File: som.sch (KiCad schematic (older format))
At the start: 1 part, among them M1 SC606T

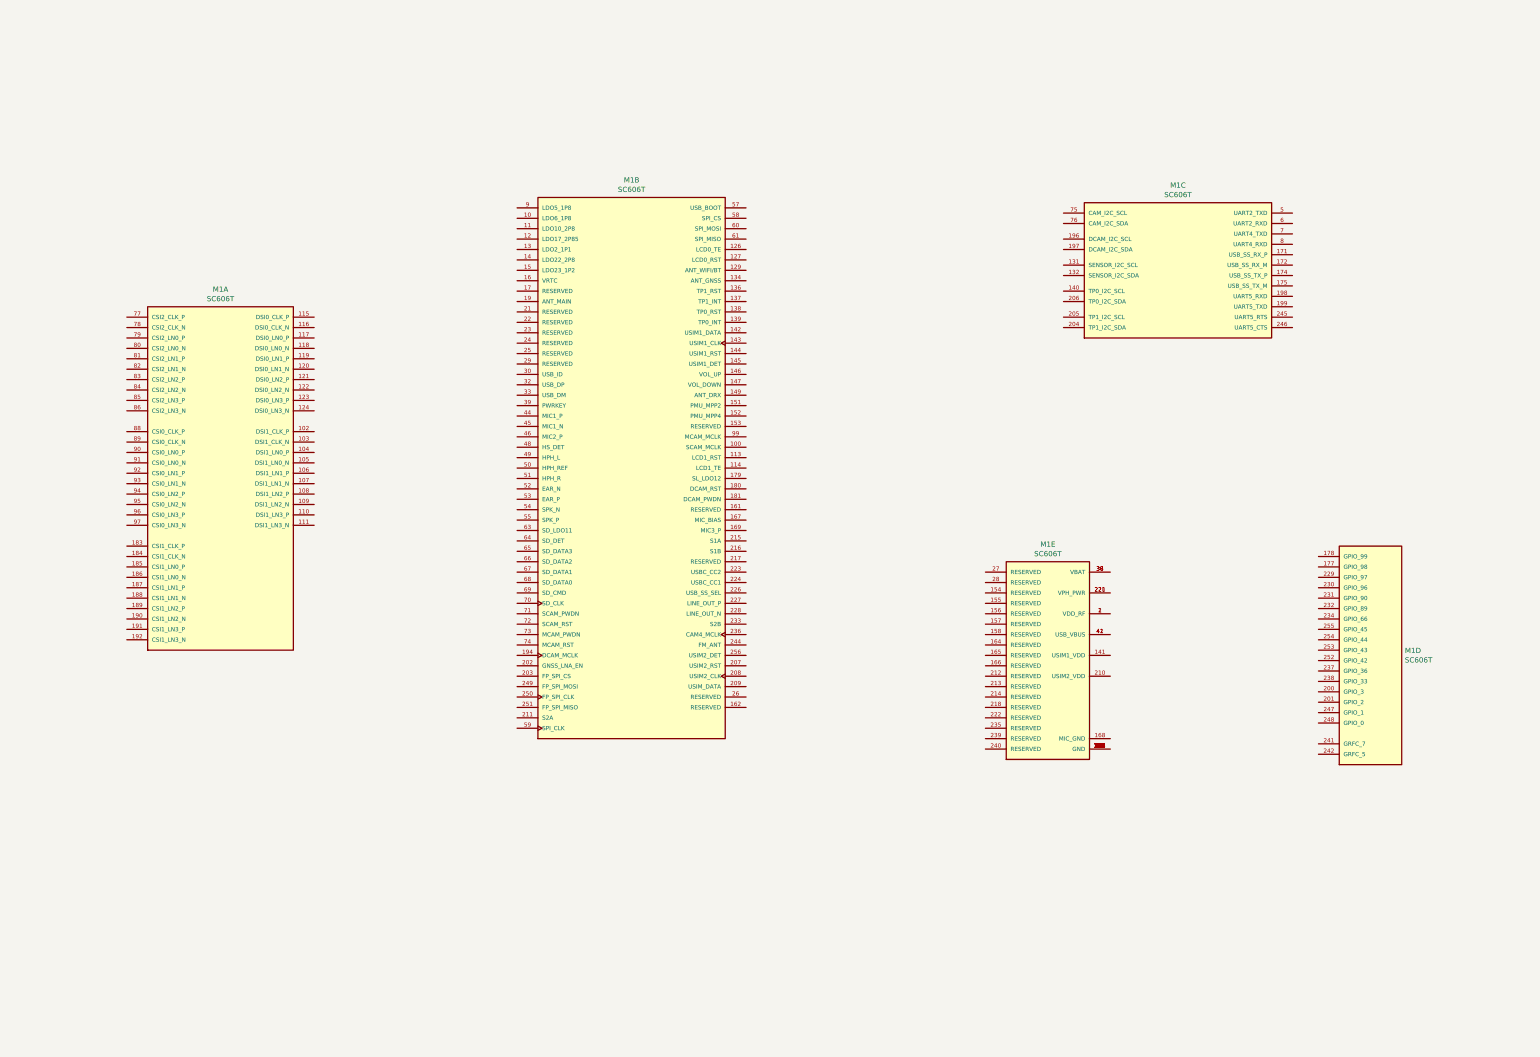
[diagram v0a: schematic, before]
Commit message: Creating schematic of SoM power supply elements
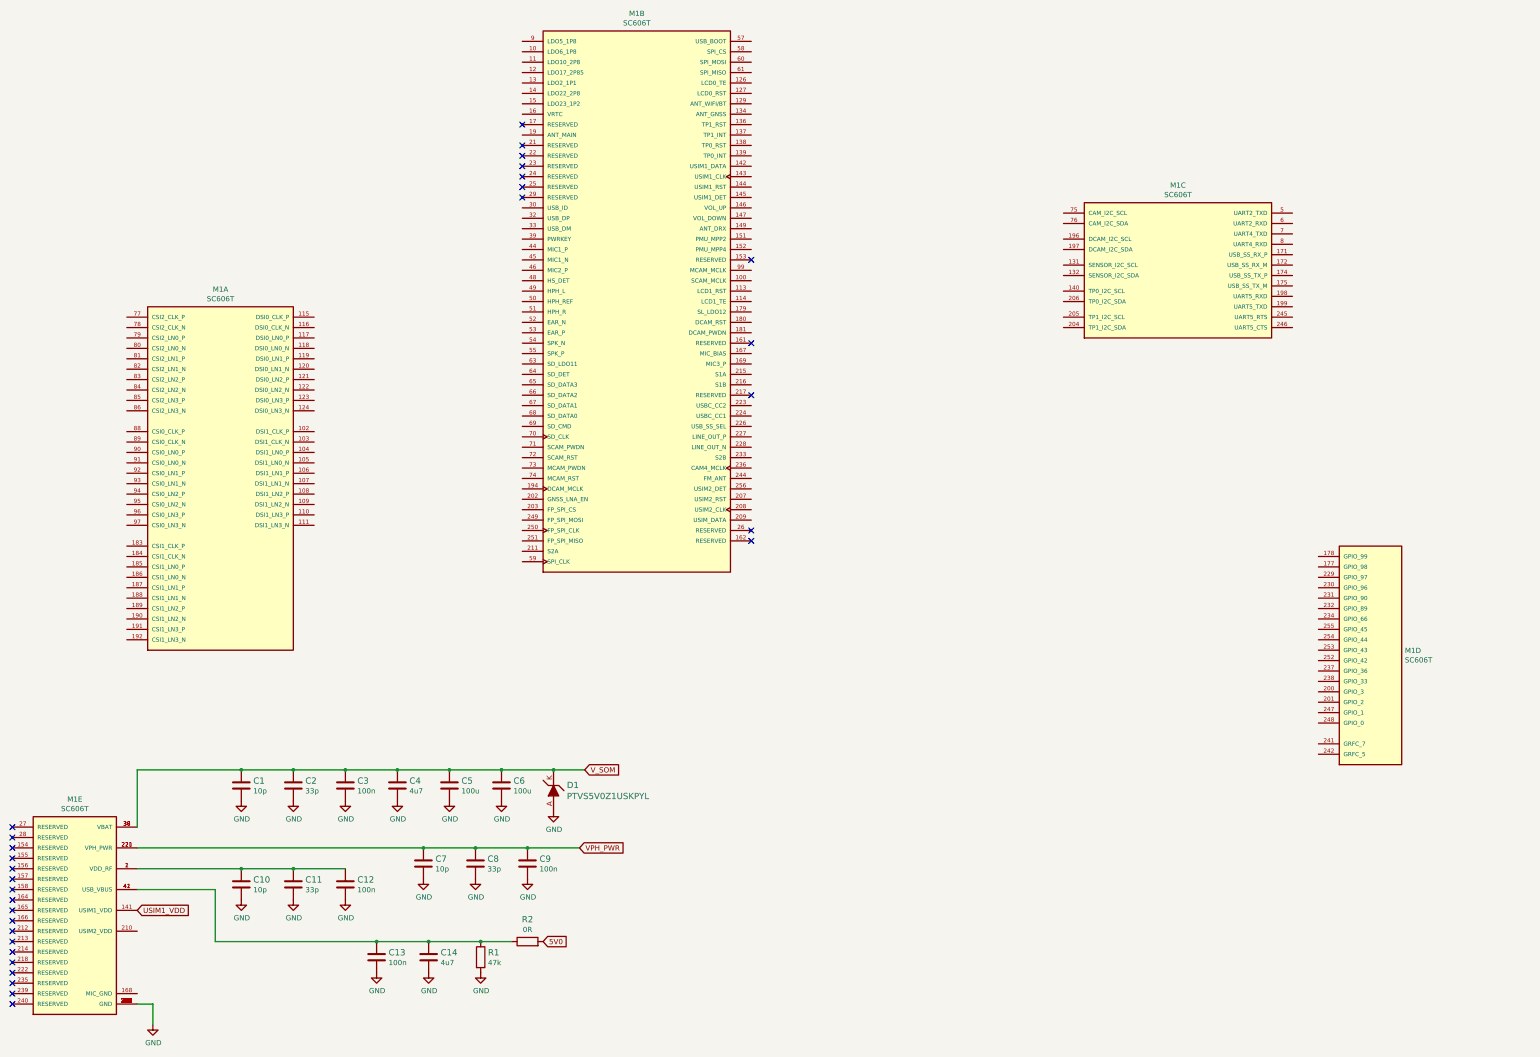
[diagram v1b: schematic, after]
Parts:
- added C1, C10, C7: C_10p_0402, antmicro-footprints:0402-cap, symbol antmicroCapacitors0402:C_10p_0402
- added C11, C2, C8: C_33p_0402, antmicro-footprints:0402-cap, symbol antmicroCapacitors0402:C_33p_0402
- added C12, C13, C3, C9: C_100n_0402, antmicro-footprints:0402-cap, symbol antmicroCapacitors0402:C_100n_0402
- added C14, C4: C_4u7_0402, antmicro-footprints:0402-cap, symbol antmicroCapacitors0402:C_4u7_0402
- added C5, C6: C_100u_1206, antmicro-footprints:1206-cap, symbol antmicroCapacitorsmisc:C_100u_1206
- added D1: PTVS5V0Z1USKPYL, antmicro-footprints:SOD-964, symbol antmicroTVSDiodes:PTVS5V0Z1USKPYL
- added R1: R_47k_0402, antmicro-footprints:0402-res, symbol antmicroResistors0402:R_47k_0402
- added R2: R_0R_0402, antmicro-footprints:0402-res, symbol antmicroResistors0402:R_0R_0402
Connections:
- net at M1.1 (VDD_RF), M1.2 (VDD_RF): now also C10.1, C11.1, C12.1
- net GND: now reaches M1.101 (GND), M1.112 (GND), M1.125 (GND), M1.128 (GND), M1.130 (GND), M1.133 (GND), M1.135 (GND), M1.148 (GND), M1.150 (GND), M1.159 (GND), M1.160 (GND), M1.163 (GND), M1.170 (GND), M1.173 (GND), M1.176 (GND), M1.18 (GND), M1.182 (GND), M1.193 (GND), M1.195 (GND), M1.20 (GND), M1.219 (GND), M1.225 (GND), M1.243 (GND), M1.257 (GND), M1.258 (GND), M1.259 (GND), M1.260 (GND), M1.261 (GND), M1.262 (GND), M1.263 (GND), M1.264 (GND), M1.265 (GND), M1.266 (GND), M1.267 (GND), M1.268 (GND), M1.269 (GND), M1.270 (GND), M1.271 (GND), M1.272 (GND), M1.273 (GND), M1.274 (GND), M1.275 (GND), M1.276 (GND), M1.277 (GND), M1.278 (GND), M1.279 (GND), M1.280 (GND), M1.281 (GND), M1.282 (GND), M1.283 (GND), M1.284 (GND), M1.285 (GND), M1.286 (GND), M1.287 (GND), M1.288 (GND), M1.289 (GND), M1.290 (GND), M1.291 (GND), M1.292 (GND), M1.293 (GND), M1.294 (GND), M1.295 (GND), M1.296 (GND), M1.297 (GND), M1.298 (GND), M1.299 (GND), M1.3 (GND), M1.300 (GND), M1.301 (GND), M1.302 (GND), M1.303 (GND), M1.304 (GND), M1.305 (GND), M1.306 (GND), M1.307 (GND), M1.308 (GND), M1.309 (GND), M1.31 (GND), M1.310 (GND), M1.311 (GND), M1.312 (GND), M1.313 (GND), M1.314 (GND), M1.315 (GND), M1.316 (GND), M1.317 (GND), M1.318 (GND), M1.319 (GND), M1.320 (GND), M1.321 (GND), M1.322 (GND), M1.323 (GND), M1.34 (GND), M1.35 (GND), M1.4 (GND), M1.40 (GND), M1.43 (GND), M1.47 (GND), M1.56 (GND), M1.62 (GND), M1.87 (GND), M1.98 (GND)
- net GND: now also C1.2, C10.2, C11.2, C12.2, C13.2, C14.2, C2.2, C3.2, C4.2, C5.2, C6.2, C7.2, C8.2, C9.2, D1.A, R1.2
- net USIM1_VDD: now reaches M1.141 (USIM1_VDD)
- net VPH_PWR: now reaches M1.220 (VPH_PWR), M1.221 (VPH_PWR)
- net VPH_PWR: now also C7.1, C8.1, C9.1
- net V_SOM: now reaches M1.36 (VBAT), M1.37 (VBAT), M1.38 (VBAT)
- net V_SOM: now also C1.1, C2.1, C3.1, C4.1, C5.1, C6.1, D1.K
- net at M1.41 (USB_VBUS), M1.42 (USB_VBUS): now also C13.1, C14.1, R1.1, R2.1
- new net 5V0: R2.2
- no-connect marks 0 -> 30
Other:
- moved on the sheet: M1B, M1E

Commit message: Add scheme for SIM card
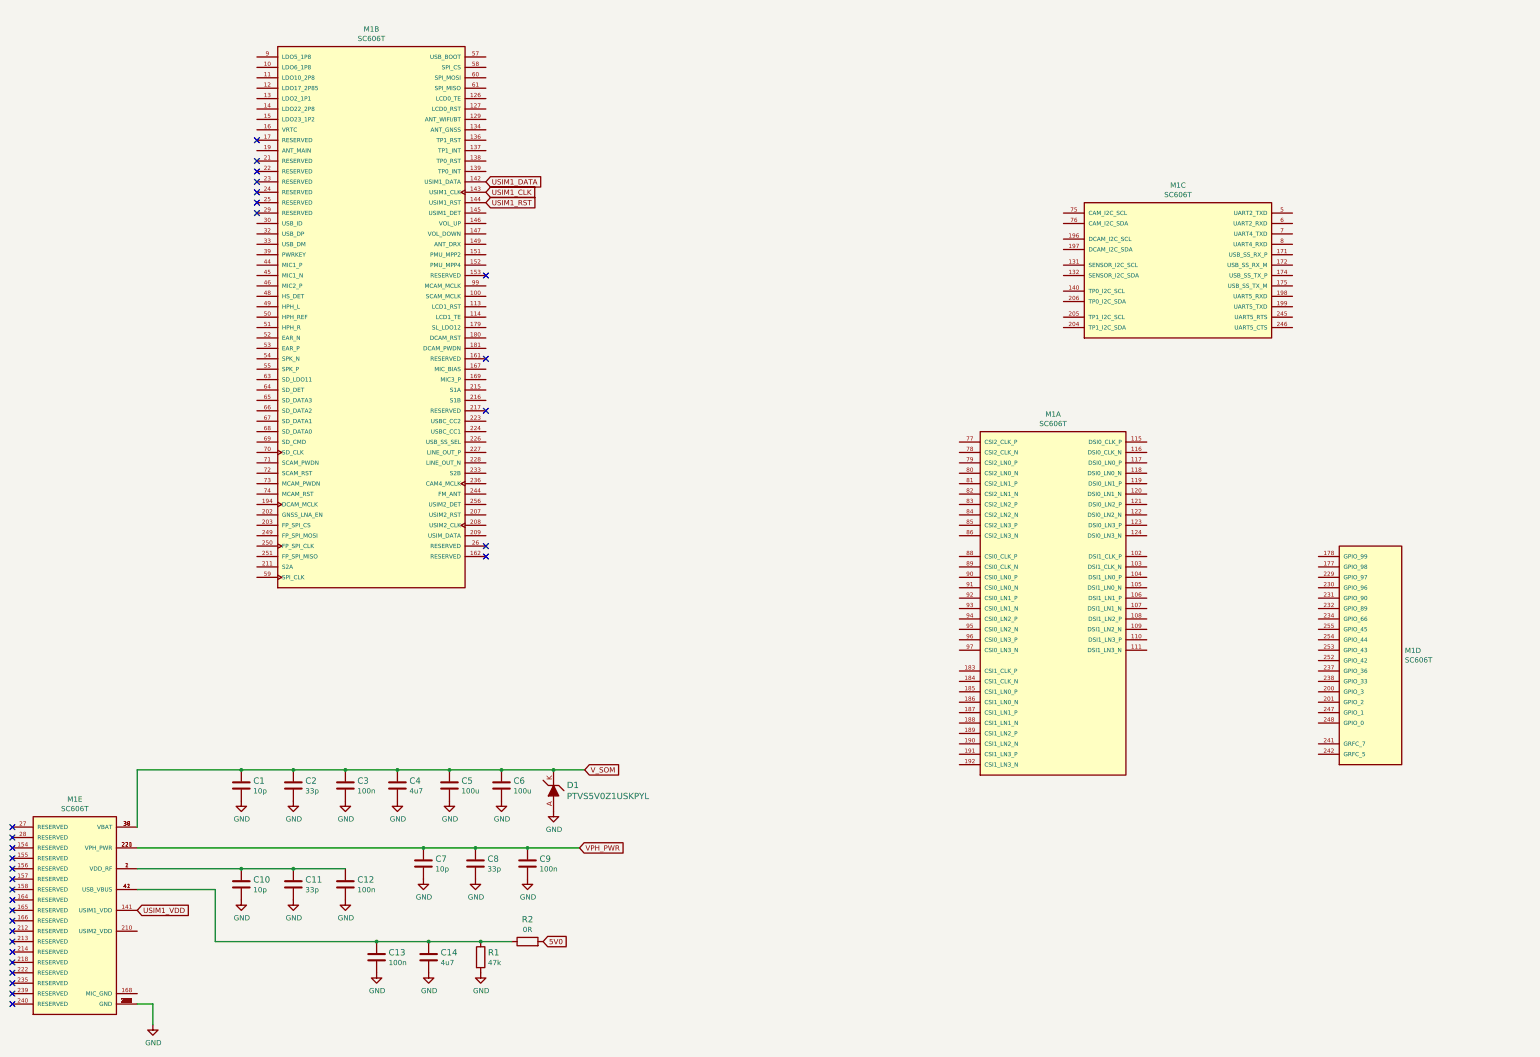
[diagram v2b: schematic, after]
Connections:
- net USIM1_DATA: now reaches M1.142 (USIM1_DATA)
- net USIM1_CLK: now reaches M1.143 (USIM1_CLK)
- net USIM1_RST: now reaches M1.144 (USIM1_RST)
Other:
- moved on the sheet: M1A, M1B
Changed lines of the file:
@@
 L antmicroModules:SC606T M1
 U 1 1 61D4A36E
-P 2800 5150
-F 0 "M1" H 2800 6917 50  0000 C CNN
-F 1 "SC606T" H 2800 6826 50  0000 C CNN
-F 2 "antmicro-footprints:QUECTEL_SC606T" H 2850 5250 50  0001 L BNN
-F 3 "" H 2800 5300 50  0001 L BNN
-F 4 "Quectel" H 2800 5300 50  0001 L BNN "Manufacturer"
-F 5 "SC606T-xx" H 2800 5300 50  0001 C CNN "MPN"
-	1    2800 5150
+P 10800 6350
+F 0 "M1" H 10800 8117 50  0000 C CNN
+F 1 "SC606T" H 10800 8026 50  0000 C CNN
+F 2 "antmicro-footprints:QUECTEL_SC606T" H 10850 6450 50  0001 L BNN
+F 3 "" H 10800 6500 50  0001 L BNN
+F 4 "Quectel" H 10800 6500 50  0001 L BNN "Manufacturer"
+F 5 "SC606T-xx" H 10800 6500 50  0001 C CNN "MPN"
+	1    10800 6350
 	1    0    0    -1
 $EndComp
@@
 NoConn ~ 800  10150
 NoConn ~ 800  10250
-NoConn ~ 5700 2000
-NoConn ~ 5700 2100
-NoConn ~ 5700 2200
-NoConn ~ 5700 2300
-NoConn ~ 5700 2400
-NoConn ~ 5700 2500
-NoConn ~ 5700 1800
-NoConn ~ 7900 5700
-NoConn ~ 7900 5800
-NoConn ~ 7900 3900
-NoConn ~ 7900 4400
-NoConn ~ 7900 3100
+NoConn ~ 3150 2150
+NoConn ~ 3150 2250
+NoConn ~ 3150 2350
+NoConn ~ 3150 2450
+NoConn ~ 3150 2550
+NoConn ~ 3150 2650
+NoConn ~ 3150 1950
+NoConn ~ 5350 5850
+NoConn ~ 5350 5950
+NoConn ~ 5350 4050
+NoConn ~ 5350 4550
+NoConn ~ 5350 3250
 $Comp
 L power:GND #PWR?
@@
 Wire Wire Line
 	2150 10250 2150 10450
-$Comp
-L antmicroModules:SC606T M1
-U 2 1 61D5D2CB
-P 6800 3300
-F 0 "M1" H 6800 5867 50  0000 C CNN
-F 1 "SC606T" H 6800 5776 50  0000 C CNN
-F 2 "antmicro-footprints:QUECTEL_SC606T" H 6850 3400 50  0001 L BNN
-F 3 "" H 6800 3450 50  0001 L BNN
-F 4 "Quectel" H 6800 3450 50  0001 L BNN "Manufacturer"
-F 5 "SC606T-xx" H 6800 3450 50  0001 C CNN "MPN"
-	2    6800 3300
-	1    0    0    -1
-$EndComp
 Text GLabel 6300 8000 2    50   Input ~ 0
 V_SOM
@@
 Wire Wire Line
 	2000 8750 4750 8750
+$Comp
+L antmicroModules:SC606T M1
+U 2 1 61D5D2CB
+P 4250 3450
+F 0 "M1" H 4250 6017 50  0000 C CNN
+F 1 "SC606T" H 4250 5926 50  0000 C CNN
+F 2 "antmicro-footprints:QUECTEL_SC606T" H 4300 3550 50  0001 L BNN
+F 3 "" H 4250 3600 50  0001 L BNN
+F 4 "Quectel" H 4250 3600 50  0001 L BNN "Manufacturer"
+F 5 "SC606T-xx" H 4250 3600 50  0001 C CNN "MPN"
+	2    4250 3450
+	1    0    0    -1
+$EndComp
+Text GLabel 5350 2350 2    50   Input ~ 0
+USIM1_DATA
+Text GLabel 5350 2450 2    50   Input ~ 0
+USIM1_CLK
+Text GLabel 5350 2550 2    50   Input ~ 0
+USIM1_RST
 $EndSCHEMATC

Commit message: Scheme for 5V Main DC/DC converter created
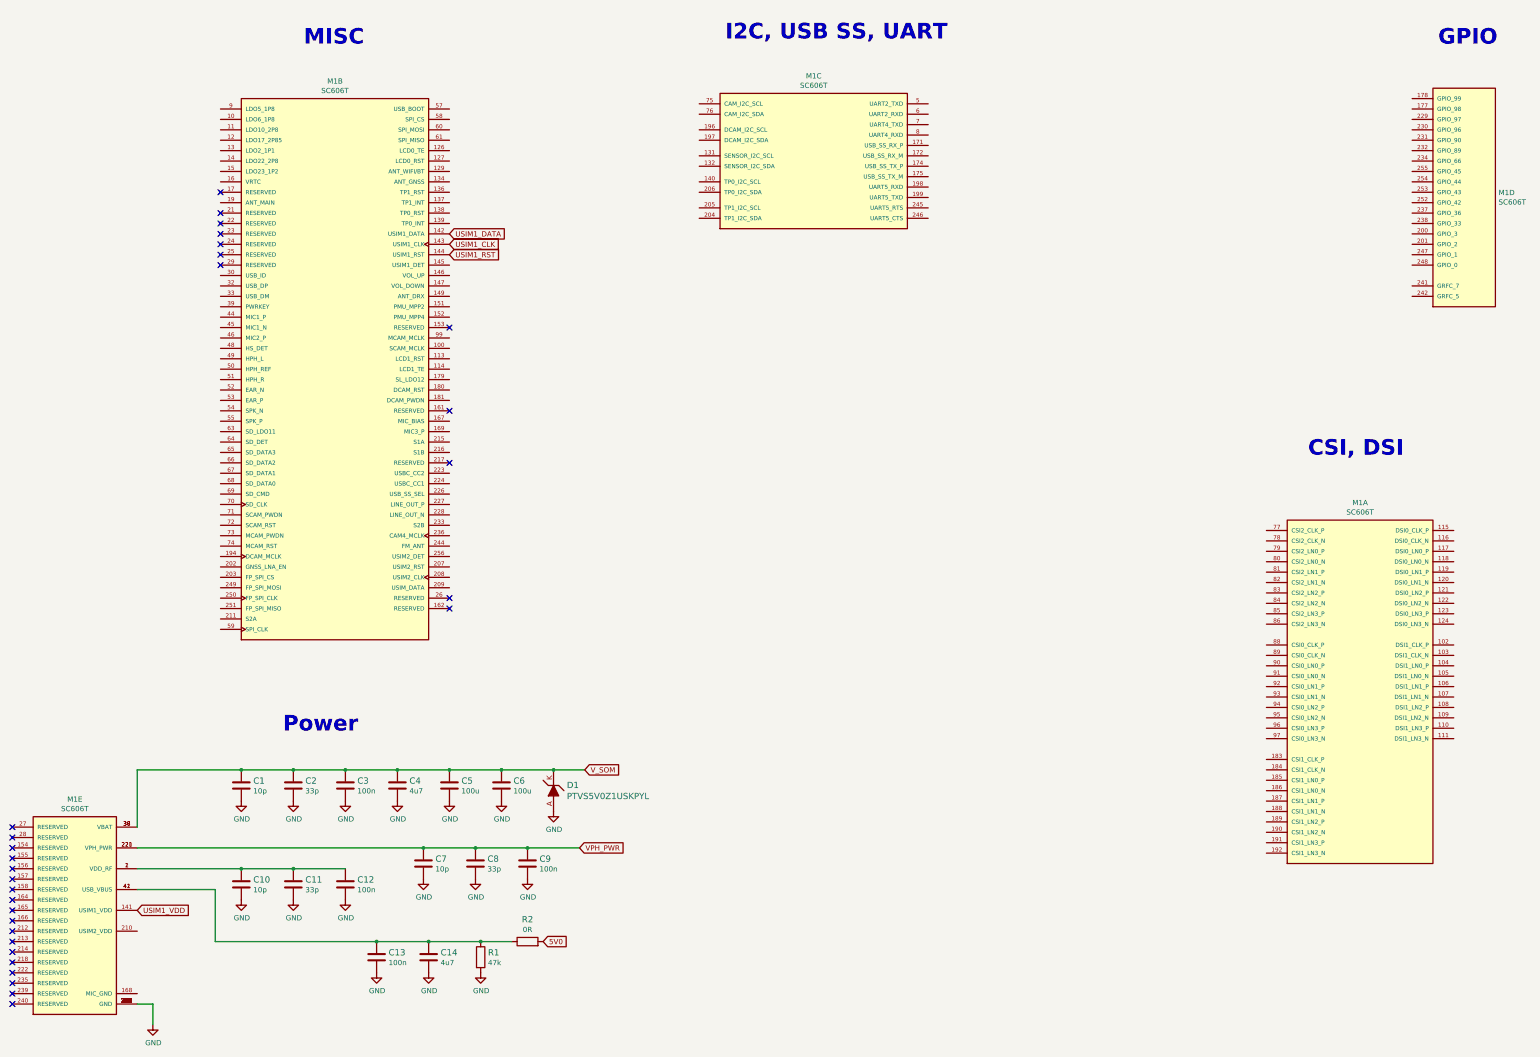
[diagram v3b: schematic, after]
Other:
- note added: "CSI, DSI"
- note added: "GPIO"
- note added: "I2C, USB SS, UART"
- note added: "MISC\n"
- note added: "Power"
- moved on the sheet: M1A, M1B, M1C, M1D
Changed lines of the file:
@@
 L antmicroModules:SC606T M1
 U 1 1 61D4A36E
-P 10800 6350
-F 0 "M1" H 10800 8117 50  0000 C CNN
-F 1 "SC606T" H 10800 8026 50  0000 C CNN
-F 2 "antmicro-footprints:QUECTEL_SC606T" H 10850 6450 50  0001 L BNN
-F 3 "" H 10800 6500 50  0001 L BNN
-F 4 "Quectel" H 10800 6500 50  0001 L BNN "Manufacturer"
-F 5 "SC606T-xx" H 10800 6500 50  0001 C CNN "MPN"
-	1    10800 6350
+P 13750 7200
+F 0 "M1" H 13750 8967 50  0000 C CNN
+F 1 "SC606T" H 13750 8876 50  0000 C CNN
+F 2 "antmicro-footprints:QUECTEL_SC606T" H 13800 7300 50  0001 L BNN
+F 3 "" H 13750 7350 50  0001 L BNN
+F 4 "Quectel" H 13750 7350 50  0001 L BNN "Manufacturer"
+F 5 "SC606T-xx" H 13750 7350 50  0001 C CNN "MPN"
+	1    13750 7200
 	1    0    0    -1
 $EndComp
@@
 L antmicroModules:SC606T M1
 U 3 1 61D62FE5
-P 12000 3200
-F 0 "M1" H 12000 4017 50  0000 C CNN
-F 1 "SC606T" H 12000 3926 50  0000 C CNN
-F 2 "antmicro-footprints:QUECTEL_SC606T" H 12050 3300 50  0001 L BNN
-F 3 "" H 12000 3350 50  0001 L BNN
-F 4 "Quectel" H 12000 3350 50  0001 L BNN "Manufacturer"
-F 5 "SC606T-xx" H 12000 3350 50  0001 C CNN "MPN"
-	3    12000 3200
+P 8500 2150
+F 0 "M1" H 8500 2967 50  0000 C CNN
+F 1 "SC606T" H 8500 2876 50  0000 C CNN
+F 2 "antmicro-footprints:QUECTEL_SC606T" H 8550 2250 50  0001 L BNN
+F 3 "" H 8500 2300 50  0001 L BNN
+F 4 "Quectel" H 8500 2300 50  0001 L BNN "Manufacturer"
+F 5 "SC606T-xx" H 8500 2300 50  0001 C CNN "MPN"
+	3    8500 2150
 	1    0    0    -1
 $EndComp
@@
 L antmicroModules:SC606T M1
 U 4 1 61D67FBA
-P 13850 6700
-F 0 "M1" H 14180 6546 50  0000 L CNN
-F 1 "SC606T" H 14180 6455 50  0000 L CNN
-F 2 "antmicro-footprints:QUECTEL_SC606T" H 13900 6800 50  0001 L BNN
-F 3 "" H 13850 6850 50  0001 L BNN
-F 4 "Quectel" H 13850 6850 50  0001 L BNN "Manufacturer"
-F 5 "SC606T-xx" H 13850 6850 50  0001 C CNN "MPN"
-	4    13850 6700
+P 14750 2300
+F 0 "M1" H 15080 2146 50  0000 L CNN
+F 1 "SC606T" H 15080 2055 50  0000 L CNN
+F 2 "antmicro-footprints:QUECTEL_SC606T" H 14800 2400 50  0001 L BNN
+F 3 "" H 14750 2450 50  0001 L BNN
+F 4 "Quectel" H 14750 2450 50  0001 L BNN "Manufacturer"
+F 5 "SC606T-xx" H 14750 2450 50  0001 C CNN "MPN"
+	4    14750 2300
 	1    0    0    -1
 $EndComp
@@
 NoConn ~ 800  10150
 NoConn ~ 800  10250
-NoConn ~ 3150 2150
-NoConn ~ 3150 2250
-NoConn ~ 3150 2350
-NoConn ~ 3150 2450
-NoConn ~ 3150 2550
-NoConn ~ 3150 2650
-NoConn ~ 3150 1950
-NoConn ~ 5350 5850
-NoConn ~ 5350 5950
-NoConn ~ 5350 4050
-NoConn ~ 5350 4550
-NoConn ~ 5350 3250
+NoConn ~ 2800 2650
+NoConn ~ 2800 2750
+NoConn ~ 2800 2850
+NoConn ~ 2800 2950
+NoConn ~ 2800 3050
+NoConn ~ 2800 3150
+NoConn ~ 2800 2450
+NoConn ~ 5000 6350
+NoConn ~ 5000 6450
+NoConn ~ 5000 4550
+NoConn ~ 5000 5050
+NoConn ~ 5000 3750
 $Comp
 L power:GND #PWR?
@@
 L antmicroModules:SC606T M1
 U 2 1 61D5D2CB
-P 4250 3450
-F 0 "M1" H 4250 6017 50  0000 C CNN
-F 1 "SC606T" H 4250 5926 50  0000 C CNN
-F 2 "antmicro-footprints:QUECTEL_SC606T" H 4300 3550 50  0001 L BNN
-F 3 "" H 4250 3600 50  0001 L BNN
-F 4 "Quectel" H 4250 3600 50  0001 L BNN "Manufacturer"
-F 5 "SC606T-xx" H 4250 3600 50  0001 C CNN "MPN"
-	2    4250 3450
-	1    0    0    -1
-$EndComp
-Text GLabel 5350 2350 2    50   Input ~ 0
+P 3900 3950
+F 0 "M1" H 3900 6517 50  0000 C CNN
+F 1 "SC606T" H 3900 6426 50  0000 C CNN
+F 2 "antmicro-footprints:QUECTEL_SC606T" H 3950 4050 50  0001 L BNN
+F 3 "" H 3900 4100 50  0001 L BNN
+F 4 "Quectel" H 3900 4100 50  0001 L BNN "Manufacturer"
+F 5 "SC606T-xx" H 3900 4100 50  0001 C CNN "MPN"
+	2    3900 3950
+	1    0    0    -1
+$EndComp
+Text GLabel 5000 2850 2    50   Input ~ 0
 USIM1_DATA
-Text GLabel 5350 2450 2    50   Input ~ 0
+Text GLabel 5000 2950 2    50   Input ~ 0
 USIM1_CLK
-Text GLabel 5350 2550 2    50   Input ~ 0
+Text GLabel 5000 3050 2    50   Input ~ 0
 USIM1_RST
+Text Notes 3400 7650 0    150  ~ 30
+Power
+Text Notes 3600 1050 0    150  ~ 30
+MISC\n
+Text Notes 7650 1000 0    150  ~ 30
+I2C, USB SS, UART
+Text Notes 14500 1050 0    150  ~ 30
+GPIO
+Text Notes 13250 5000 0    150  ~ 30
+CSI, DSI
 $EndSCHEMATC
